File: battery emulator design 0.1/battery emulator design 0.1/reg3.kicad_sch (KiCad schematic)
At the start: 12 parts, among them U5 LM741, U6 LM317_TO-220

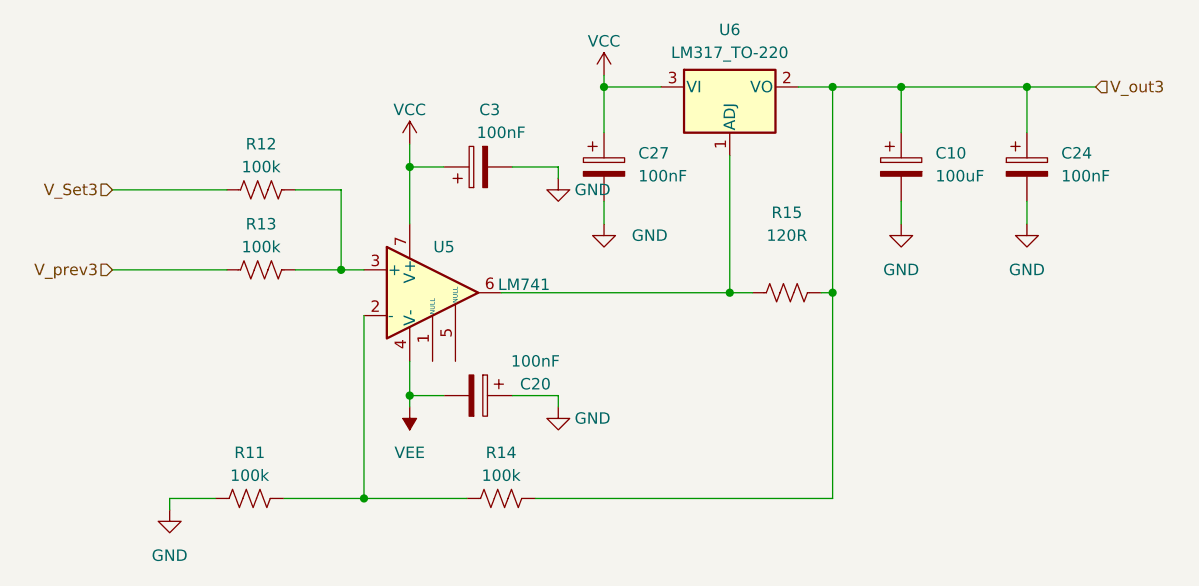
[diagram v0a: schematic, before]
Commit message: added pots to voltage buffers, other minor changes
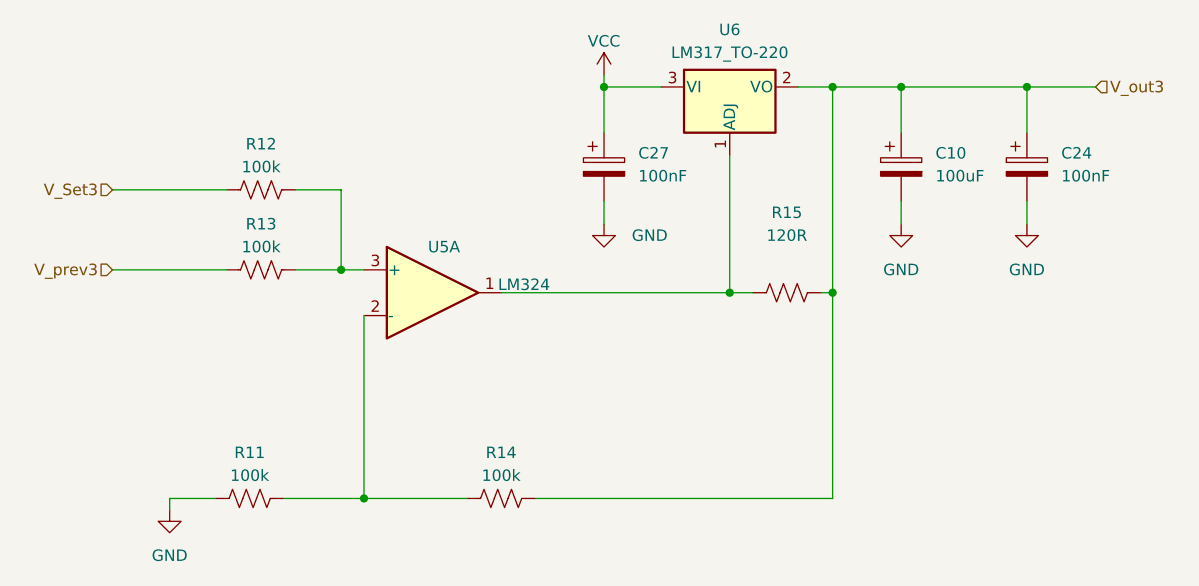
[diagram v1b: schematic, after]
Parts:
- removed C20, C3: 100nF, Capacitor_THT:C_Disc_D3.4mm_W2.1mm_P2.50mm, symbol Device:C_Polarized
- U5: value LM741 -> LM324; symbol Amplifier_Operational:LM741 -> Amplifier_Operational:LM324
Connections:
- net VCC: no longer U5.7 (V+)
- net at R15.2, U6.1 (ADJ): now also U5.1; no longer U5.6
- removed net VEE: U5.4 (V-)
